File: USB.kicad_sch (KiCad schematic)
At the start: 0 parts

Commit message: [#82055] Add USB recovery port
[#81970] add discharge circuit

[#81970] Annotation

[#81782] Annotation and clean up
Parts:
- added C147: C_1u_25V_0402, antmicro-footprints:C_0402_1005Metric, symbol antmicroCapacitors0402:C_1u_25V_0402
- added C84, C88, C93: C_100n_0402, antmicro-footprints:C_0402_1005Metric, symbol antmicroCapacitors0402:C_100n_0402
- added C91: C_4u7_25V_0402, antmicro-footprints:C_0402_1005Metric, symbol antmicroCapacitors0402:C_4u7_25V_0402
- added C92: C_10u_0402, antmicro-footprints:C_0402_1005Metric, symbol antmicroCapacitors0402:C_10u_0402
- added D19: DF2S30FS_SOD, antmicro-footprints:SOD-923, symbol antmicroTVSDiodes:DF2S30FS_SOD
- added D20: LED_G_0603_LTST-C190GKT, antmicro-footprints:LED_0603_1608Metric_G, symbol antmicroLEDIndicationDiscrete:LED_G_0603_LTST-C190GKT
- added J2: USB-C_GCT_USB4105-GF-A, antmicro-footprints:USB-C_Receptacle_GCT_USB4105-GF-A, symbol antmicroUSBConnectors:USB-C_GCT_USB4105-GF-A
- added Q1: PJE138K, antmicro-footprints:SOT-523, symbol antmicroTransistorsFETsMOSFETsSingle:PJE138K
- added R1: R_4k7_0402, antmicro-footprints:R_0402_1005Metric, symbol antmicroResistors0402:R_4k7_0402
- added R2, R5, R88, R95: R_10k_0402, antmicro-footprints:R_0402_1005Metric, symbol antmicroResistors0402:R_10k_0402
- added R91, R93: R_0R_0402, antmicro-footprints:R_0402_1005Metric, symbol antmicroResistors0402:R_0R_0402
- added R97: R_2k2_0402, antmicro-footprints:R_0402_1005Metric, symbol antmicroResistors0402:R_2k2_0402
- added U1: TPD4E05U06QDQARQ1, antmicro-footprints:USON-10_2.5x1mm_P0.5mm, symbol antmicroTVSDiodes:TPD4E05U06QDQARQ1
- added U16: AP22615A_TSOT26, antmicro-footprints:TSOT23-6, symbol antmicroPMICPowerDistributionSwitchesLoadDrivers:AP22615A_TSOT26
- added U2: TPS65988DHRSHR, antmicro-footprints:IC_TPS65987DDHRSHR, symbol antmicroInterfaceControllers:TPS65988DHRSHR
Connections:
- new net: R93.2, R95.2, U16.4 (EN)
- new net: C147.1, C93.1, D19.1 (C), J2.A4 (VBUS), J2.A9 (VBUS), J2.B4 (VBUS), J2.B9 (VBUS), R1.1, U16.1 (OUT), U2.3 (VBUS2)
- new net: D20.2 (A), R1.2
- new net: J2.A5 (CC_{1}), U1.1, U1.10, U2.45 (C2_CC1)
- new net: J2.B5 (CC_{2}), U1.2, U1.9, U2.47 (C2_CC2)
- new net: U2.52 (DRAIN2), U2.56 (DRAIN2), U2.57 (DRAIN2), U2.7 (DRAIN2)
- new net: R97.2, U16.5 (ISET)
- new net +3V3: R2.2, R88.2
- new net +5V: C88.1, C92.1, R91.2, U16.6 (IN), U2.46 (PP2_CABLE)
- new net FORCE_RECOVERY_N: Q1.3 (D), R2.1
- new net GND: C147.2, C84.2, C88.2, C91.2, C92.2, C93.2, D19.2 (A), D20.1 (C), J2.A1 (GND), J2.A12 (GND), J2.B1 (GND), J2.B12 (GND), J2.SH, Q1.2 (S), R5.1, R95.1, R97.1, U1.3, U1.8, U16.2 (GND)
- new net GPIO21: Q1.1 (G), R5.2, U2.55 (C2_USB_N/GPIO21)
- new net USB0_D+: J2.A6 (D_{A}+), J2.B6 (D_{B}+), U1.4, U1.7
- new net USB0_D-: J2.A7 (D_{A}-), J2.B7 (D_{B}-), U1.5, U1.6
- new net USBC1_5V_PEN: R91.1, R93.1
- new net USBC2_FLG: R88.1, U16.3 (FLG)
- new net USBPD0_HV: C84.1, C91.1, U2.1 (PP_HV2)
- no-connect marks 0 -> 4
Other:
- note added: "USB Port 0 Recovery"

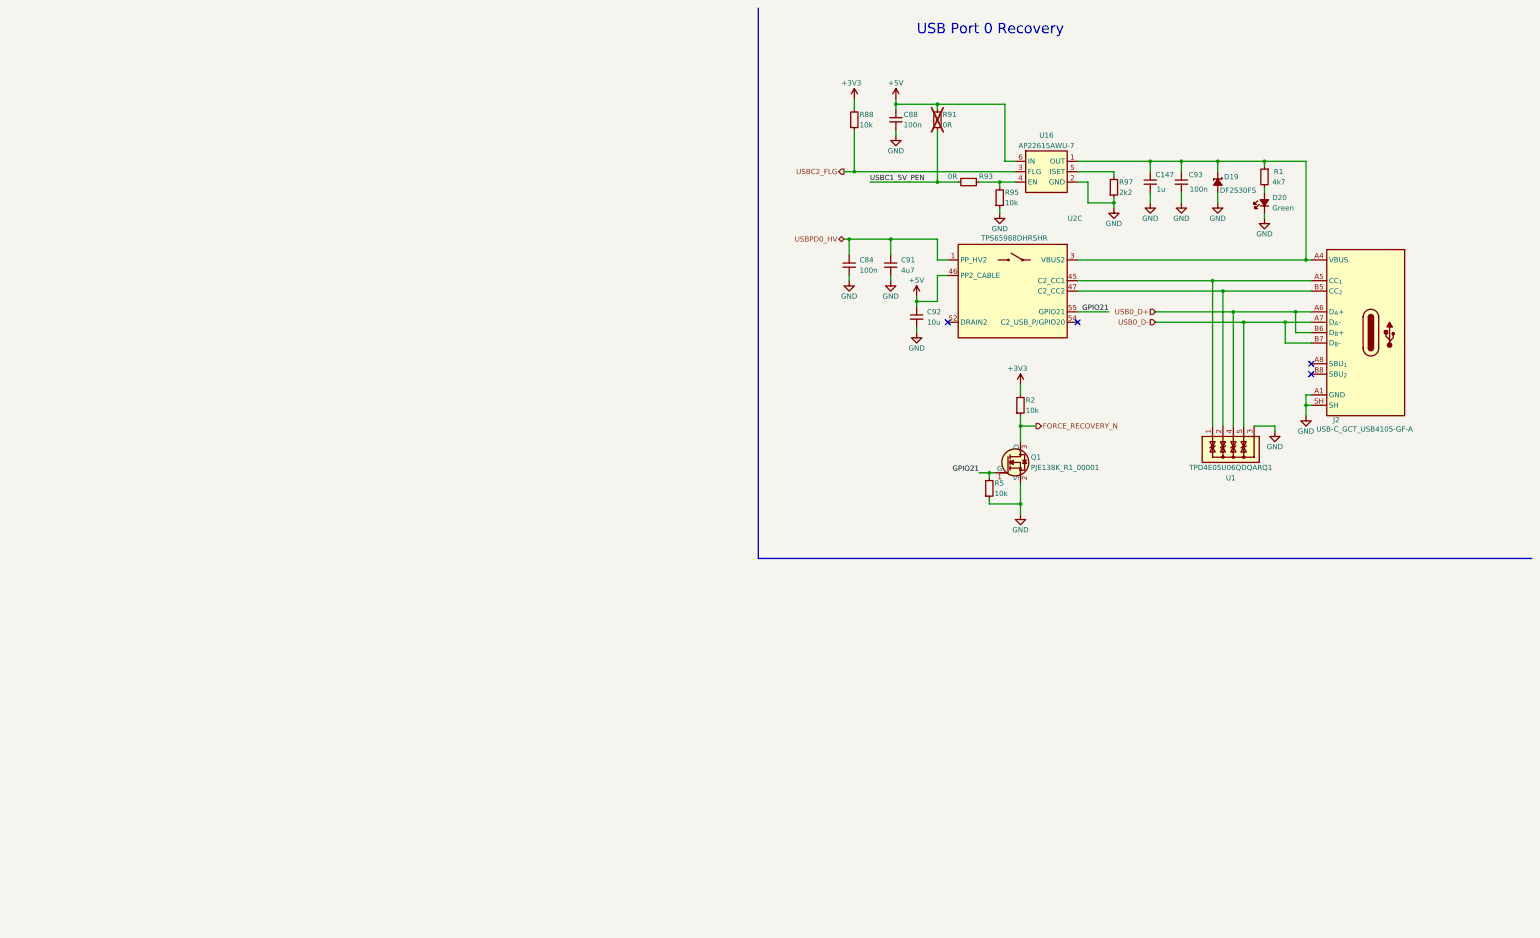
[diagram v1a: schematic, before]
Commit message: [#81970] Finalize connecting SFP+ to SOM
[#82054] Update SoM pins definitions

[#82054] Continue work on I2C

[#82330] Clean up

[#81970] Add SFP sheet and power section

[#82330] Annotation and clean up
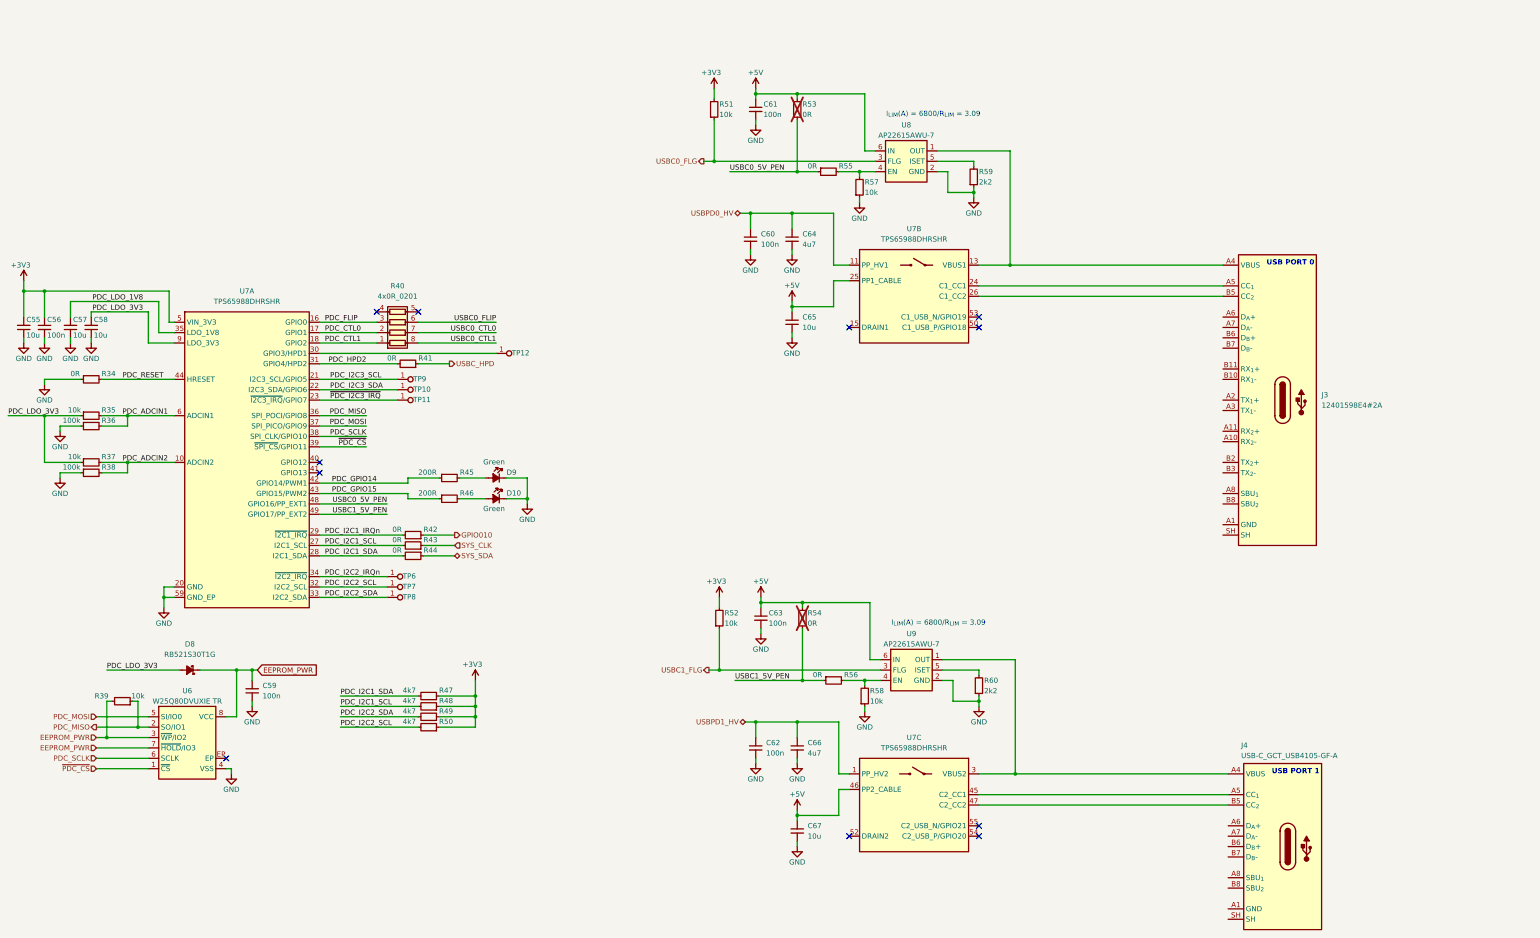
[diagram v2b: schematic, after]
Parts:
- removed C147: C_1u_25V_0402, antmicro-footprints:C_0402_1005Metric, symbol antmicroCapacitors0402:C_1u_25V_0402
- removed C93: C_100n_0402, antmicro-footprints:C_0402_1005Metric, symbol antmicroCapacitors0402:C_100n_0402
- removed D19: DF2S30FS_SOD, antmicro-footprints:SOD-923, symbol antmicroTVSDiodes:DF2S30FS_SOD
- removed D20: LED_G_0603_LTST-C190GKT, antmicro-footprints:LED_0603_1608Metric_G, symbol antmicroLEDIndicationDiscrete:LED_G_0603_LTST-C190GKT
- removed J2: USB-C_GCT_USB4105-GF-A, antmicro-footprints:USB-C_Receptacle_GCT_USB4105-GF-A, symbol antmicroUSBConnectors:USB-C_GCT_USB4105-GF-A
- removed Q1: PJE138K, antmicro-footprints:SOT-523, symbol antmicroTransistorsFETsMOSFETsSingle:PJE138K
- removed R1: R_4k7_0402, antmicro-footprints:R_0402_1005Metric, symbol antmicroResistors0402:R_4k7_0402
- removed R2, R5: R_10k_0402, antmicro-footprints:R_0402_1005Metric, symbol antmicroResistors0402:R_10k_0402
- removed R97: R_2k2_0402, antmicro-footprints:R_0402_1005Metric, symbol antmicroResistors0402:R_2k2_0402
- removed U1: TPD4E05U06QDQARQ1, antmicro-footprints:USON-10_2.5x1mm_P0.5mm, symbol antmicroTVSDiodes:TPD4E05U06QDQARQ1
- removed U2: TPS65988DHRSHR, antmicro-footprints:IC_TPS65987DDHRSHR, symbol antmicroInterfaceControllers:TPS65988DHRSHR
- added C55, C57, C58, C65: C_10u_0402, antmicro-footprints:C_0402_1005Metric, symbol antmicroCapacitors0402:C_10u_0402
- added C56, C59, C60, C61: C_100n_0402, antmicro-footprints:C_0402_1005Metric, symbol antmicroCapacitors0402:C_100n_0402
- added C64: C_4u7_25V_0402, antmicro-footprints:C_0402_1005Metric, symbol antmicroCapacitors0402:C_4u7_25V_0402
- added D10, D9: LED_G_0603_LTST-C190GKT, antmicro-footprints:LED_0603_1608Metric_G, symbol antmicroLEDIndicationDiscrete:LED_G_0603_LTST-C190GKT
- added D8: RB521S30T1G, antmicro-footprints:SOD-523, symbol antmicroDiodesRectifiersSingle:RB521S30T1G
- added J3: USB-C_Amphenol_12401598E4, antmicro-footprints:USB-C_Receptacle_Amphenol_12401598E4, symbol antmicroUSBConnectors:USB-C_Amphenol_12401598E4
- added J4: USB-C_GCT_USB4105-GF-A, antmicro-footprints:USB-C_Receptacle_GCT_USB4105-GF-A, symbol antmicroUSBConnectors:USB-C_GCT_USB4105-GF-A
- added R34, R41, R42, R43, R44, R53, R55: R_0R_0402, antmicro-footprints:R_0402_1005Metric, symbol antmicroResistors0402:R_0R_0402
- added R35, R37, R39, R51, R57: R_10k_0402, antmicro-footprints:R_0402_1005Metric, symbol antmicroResistors0402:R_10k_0402
- added R36, R38: R_100k_0402, antmicro-footprints:R_0402_1005Metric, symbol antmicroResistors0402:R_100k_0402
- added R40: R_4x0R_0201_array, antmicro-footprints:R_Array_4x0201_Panasonic_EXB18V, symbol antmicroResistorNetworksArrays:R_4x0R_0201_array
- added R45, R46: R_200R_0402, antmicro-footprints:R_0402_1005Metric, symbol antmicroResistors0402:R_200R_0402
- added R47, R48, R49, R50: R_4k7_0402, antmicro-footprints:R_0402_1005Metric, symbol antmicroResistors0402:R_4k7_0402
- added R59, R60: R_2k2_0402, antmicro-footprints:R_0402_1005Metric, symbol antmicroResistors0402:R_2k2_0402
- added TP10, TP11, TP12, TP6, TP7, TP8, TP9: TP_0.75mm_SMD, antmicro-footprints:TP_SMD_0.75mm, symbol antmicroTestPoints:TP_0.75mm_SMD
- added U6: W25Q80DV_USON, antmicro-footprints:USON-8_2x3mm_P0.5mm, symbol antmicroMemory:W25Q80DV_USON
- added U7: TPS65988DHRSHR, antmicro-footprints:IC_TPS65987DDHRSHR, symbol antmicroInterfaceControllers:TPS65988DHRSHR
- added U8: AP22615A_TSOT26, antmicro-footprints:TSOT23-6, symbol antmicroPMICPowerDistributionSwitchesLoadDrivers:AP22615A_TSOT26
- renumbered C84 to C62, C88 to C63, C91 to C66, C92 to C67, R88 to R52, R91 to R54, R93 to R56, R95 to R58, U16 to U9
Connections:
- net +3V3: now also C55.2, C56.1, R47.1, R48.1, R49.1, R50.1, R51.2, U7.5 (VIN_3V3)
- net +5V: now also C61.1, C65.1, R53.2, U7.25 (PP1_CABLE), U7.46 (PP2_CABLE), U8.6 (IN)
- net GND: now also C55.1, C56.2, C57.1, C58.1, C59.1, C60.2, C61.2, C64.2, C65.2, D10.1 (C), D9.1 (C), R34.1, R36.1, R38.1, R57.1, R59.1, R60.1, U6.4 (VSS), U7.20 (GND), U7.51 (GND), U7.59 (GND_EP), U8.2 (GND)
- net USBC1_5V_PEN: now also U7.49 (GPIO17/PP_EXT2)
- net USBPD0_HV: now also C60.1, C64.1, U7.11 (PP_HV1); no longer C62.1, C66.1
- net at U9.1 (OUT): now also J4.A4 (VBUS), J4.A9 (VBUS), J4.B4 (VBUS), J4.B9 (VBUS), U7.3 (VBUS2)
- net at U9.5 (ISET): now also R60.2
- net USBC2_FLG renamed USBC1_FLG
- new net: R59.2, U8.5 (ISET)
- new net: D9.2 (A), R45.2
- new net: J3.A4 (VBUS), J3.A9 (VBUS), J3.B4 (VBUS), J3.B9 (VBUS), U7.13 (VBUS1), U8.1 (OUT)
- new net: R55.2, R57.2, U8.4 (EN)
- new net: TP12.1, U7.30 (GPIO3/HPD1)
- new net: U7.15 (DRAIN1), U7.19 (DRAIN1), U7.58 (DRAIN1), U7.8 (DRAIN1)
- new net: J3.A5 (CC_{1}), U7.24 (C1_CC1)
- new net: J3.B5 (CC_{2}), U7.26 (C1_CC2)
- new net: J3.A1 (GND), J3.A12 (GND), J3.B1 (GND), J3.B12 (GND)
- new net: D10.2 (A), R46.2
- new net: J4.A1 (GND), J4.A12 (GND), J4.B1 (GND), J4.B12 (GND)
- new net: J4.A5 (CC_{1}), U7.45 (C2_CC1)
- new net: J4.B5 (CC_{2}), U7.47 (C2_CC2)
- new net: U7.52 (DRAIN2), U7.56 (DRAIN2), U7.57 (DRAIN2), U7.7 (DRAIN2)
- new net EEPROM_PWR: C59.2, D8.1 (C), R39.2, U6.3 (~{WP}/IO2), U6.7 (~{HOLD}/IO3), U6.8 (VCC)
- new net GPIO010: R42.1
- new net PDC_ADCIN1: R35.2, R36.2, U7.6 (ADCIN1)
- new net PDC_ADCIN2: R37.2, R38.2, U7.10 (ADCIN2)
- new net PDC_CTL0: R40.2 (R2.1), U7.17 (GPIO1)
- new net PDC_CTL1: R40.1 (R1.1), U7.18 (GPIO2)
- new net PDC_FLIP: R40.3 (R3.1), U7.16 (GPIO0)
- new net PDC_GPIO14: R45.1, U7.42 (GPIO14/PWM1)
- new net PDC_GPIO15: R46.1, U7.43 (GPIO15/PWM2)
- new net PDC_HPD2: R41.2, U7.31 (GPIO4/HPD2)
- new net PDC_I2C1_IRQn: R42.2, U7.29 (~{I2C1_IRQ})
- new net PDC_I2C1_SCL: R43.2, R48.2, U7.27 (I2C1_SCL)
- new net PDC_I2C1_SDA: R44.2, R47.2, U7.28 (I2C1_SDA)
- new net PDC_I2C2_IRQn: TP6.1, U7.34 (~{I2C2_IRQ})
- new net PDC_I2C2_SCL: R50.2, TP7.1, U7.32 (I2C2_SCL)
- new net PDC_I2C2_SDA: R49.2, TP8.1, U7.33 (I2C2_SDA)
- new net PDC_I2C3_SCL: TP9.1, U7.21 (I2C3_SCL/GPIO5)
- new net PDC_I2C3_SDA: TP10.1, U7.22 (I2C3_SDA/GPIO6)
- new net PDC_LDO_1V8: C57.2, U7.35 (LDO_1V8)
- new net PDC_LDO_3V3: C58.2, D8.2 (A), R35.1, R37.1, U7.9 (LDO_3V3)
- new net PDC_MISO: R39.1, U6.2 (SO/IO1), U7.36 (SPI_POCI/GPIO8)
- new net PDC_MOSI: U6.5 (SI/IO0), U7.37 (SPI_PICO/GPIO9)
- new net PDC_RESET: R34.2, U7.44 (HRESET)
- new net PDC_SCLK: U6.6 (SCLK), U7.38 (SPI_CLK/GPIO10)
- new net SYS_CLK: R43.1
- new net SYS_SDA: R44.1
- new net USBC0_5V_PEN: R53.1, R55.1, U7.48 (GPIO16/PP_EXT1)
- new net USBC0_CTL0: R40.7 (R2.2)
- new net USBC0_CTL1: R40.8 (R1.2)
- new net USBC0_FLG: R51.1, U8.3 (FLG)
- new net USBC0_FLIP: R40.6 (R3.2)
- new net USBC_HPD: R41.1
- new net USBPD1_HV: C62.1, C66.1, U7.1 (PP_HV2)
- new net ~{PDC_CS}: U6.1 (~{CS}), U7.39 (~{SPI_CS}/GPIO11)
- new net ~{PDC_I2C3_IRQ}: TP11.1, U7.23 (~{I2C3_IRQ}/GPIO7)
- no-connect marks 4 -> 11
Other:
- note added: "I_{LIM}(A) = 6800/R_{LIM} = 3.09"
- note added: "USB PORT 0"
- note added: "USB PORT 1"
- note removed: "USB Port 0 Recovery"
- moved on the sheet: C62, C63, C66, C67, R52, R54, R56, R58, U9

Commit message: [#82055] Revert back to USB-PD on DP and Debug ports
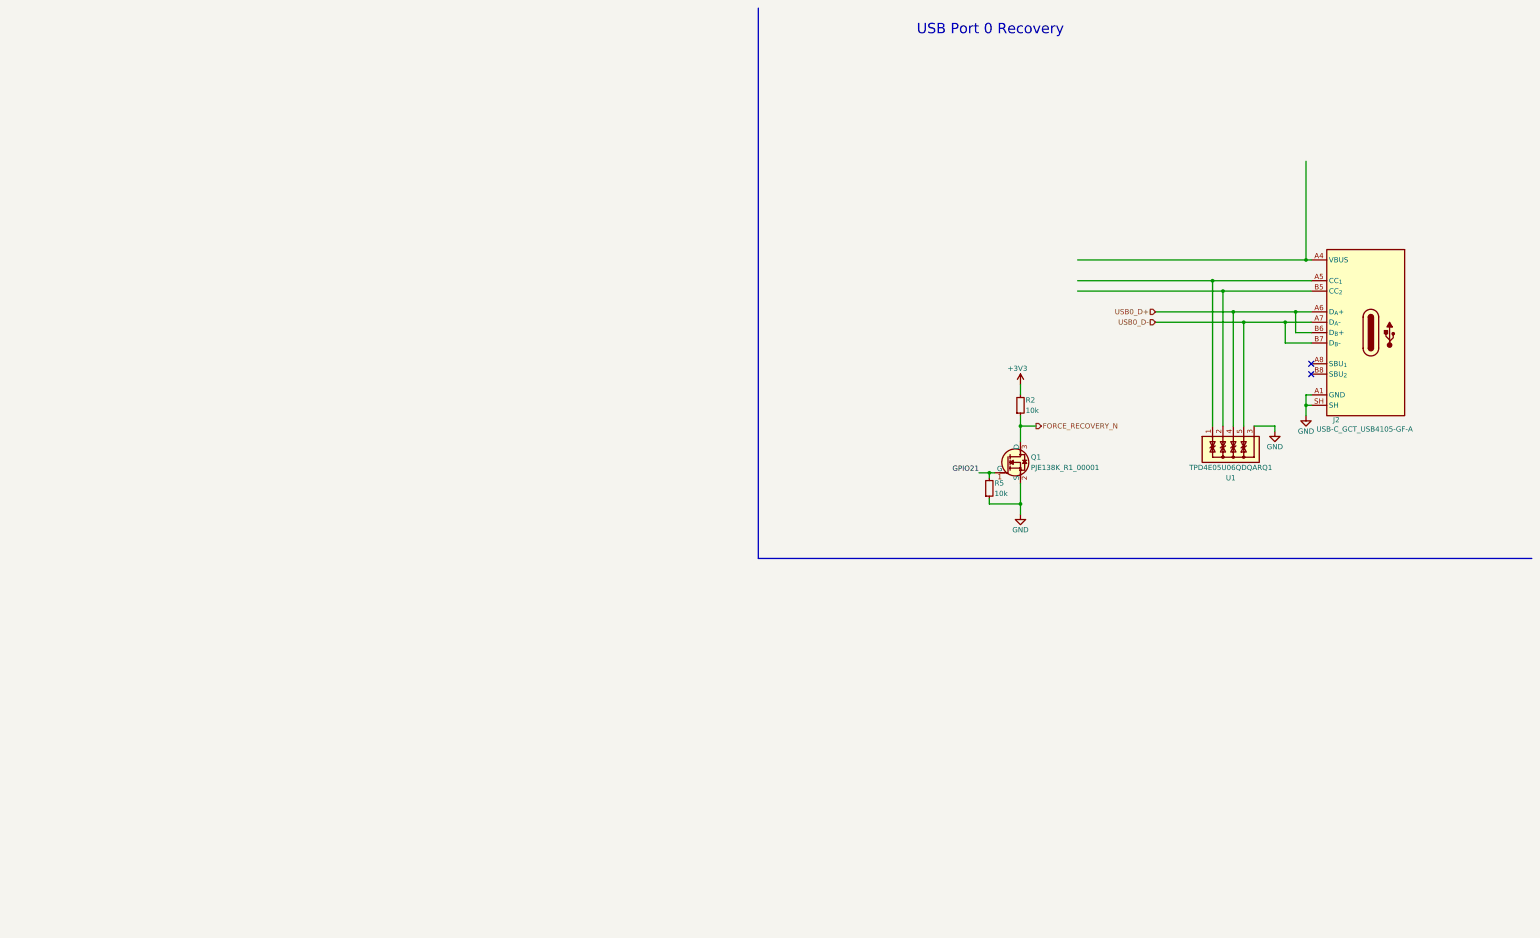
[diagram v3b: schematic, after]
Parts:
- removed C55, C57, C58, C65, C67: C_10u_0402, antmicro-footprints:C_0402_1005Metric, symbol antmicroCapacitors0402:C_10u_0402
- removed C56, C59, C60, C61, C62, C63: C_100n_0402, antmicro-footprints:C_0402_1005Metric, symbol antmicroCapacitors0402:C_100n_0402
- removed C64, C66: C_4u7_25V_0402, antmicro-footprints:C_0402_1005Metric, symbol antmicroCapacitors0402:C_4u7_25V_0402
- removed D10, D9: LED_G_0603_LTST-C190GKT, antmicro-footprints:LED_0603_1608Metric_G, symbol antmicroLEDIndicationDiscrete:LED_G_0603_LTST-C190GKT
- removed D8: RB521S30T1G, antmicro-footprints:SOD-523, symbol antmicroDiodesRectifiersSingle:RB521S30T1G
- removed J3: USB-C_Amphenol_12401598E4, antmicro-footprints:USB-C_Receptacle_Amphenol_12401598E4, symbol antmicroUSBConnectors:USB-C_Amphenol_12401598E4
- removed J4: USB-C_GCT_USB4105-GF-A, antmicro-footprints:USB-C_Receptacle_GCT_USB4105-GF-A, symbol antmicroUSBConnectors:USB-C_GCT_USB4105-GF-A
- removed R34, R41, R42, R43, R44, R53, R54, R55, R56: R_0R_0402, antmicro-footprints:R_0402_1005Metric, symbol antmicroResistors0402:R_0R_0402
- removed R35, R37, R39, R51, R52, R57, R58: R_10k_0402, antmicro-footprints:R_0402_1005Metric, symbol antmicroResistors0402:R_10k_0402
- removed R36, R38: R_100k_0402, antmicro-footprints:R_0402_1005Metric, symbol antmicroResistors0402:R_100k_0402
- removed R40: R_4x0R_0201_array, antmicro-footprints:R_Array_4x0201_Panasonic_EXB18V, symbol antmicroResistorNetworksArrays:R_4x0R_0201_array
- removed R45, R46: R_200R_0402, antmicro-footprints:R_0402_1005Metric, symbol antmicroResistors0402:R_200R_0402
- removed R47, R48, R49, R50: R_4k7_0402, antmicro-footprints:R_0402_1005Metric, symbol antmicroResistors0402:R_4k7_0402
- removed R59, R60: R_2k2_0402, antmicro-footprints:R_0402_1005Metric, symbol antmicroResistors0402:R_2k2_0402
- removed TP10, TP11, TP12, TP6, TP7, TP8, TP9: TP_0.75mm_SMD, antmicro-footprints:TP_SMD_0.75mm, symbol antmicroTestPoints:TP_0.75mm_SMD
- removed U6: W25Q80DV_USON, antmicro-footprints:USON-8_2x3mm_P0.5mm, symbol antmicroMemory:W25Q80DV_USON
- removed U7: TPS65988DHRSHR, antmicro-footprints:IC_TPS65987DDHRSHR, symbol antmicroInterfaceControllers:TPS65988DHRSHR
- removed U8, U9: AP22615A_TSOT26, antmicro-footprints:TSOT23-6, symbol antmicroPMICPowerDistributionSwitchesLoadDrivers:AP22615A_TSOT26
- added J2: USB-C_GCT_USB4105-GF-A, antmicro-footprints:USB-C_Receptacle_GCT_USB4105-GF-A, symbol antmicroUSBConnectors:USB-C_GCT_USB4105-GF-A
- added Q1: PJE138K, antmicro-footprints:SOT-523, symbol antmicroTransistorsFETsMOSFETsSingle:PJE138K
- added R2, R5: R_10k_0402, antmicro-footprints:R_0402_1005Metric, symbol antmicroResistors0402:R_10k_0402
- added U1: TPD4E05U06QDQARQ1, antmicro-footprints:USON-10_2.5x1mm_P0.5mm, symbol antmicroTVSDiodes:TPD4E05U06QDQARQ1
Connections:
- net +3V3: now also R2.2
- net GND: now also J2.A1 (GND), J2.A12 (GND), J2.B1 (GND), J2.B12 (GND), J2.SH, Q1.2 (S), R5.1, U1.3, U1.8
- new net: J2.A4 (VBUS), J2.A9 (VBUS), J2.B4 (VBUS), J2.B9 (VBUS)
- new net: J2.A5 (CC_{1}), U1.1, U1.10
- new net: J2.B5 (CC_{2}), U1.2, U1.9
- new net FORCE_RECOVERY_N: Q1.3 (D), R2.1
- new net GPIO21: Q1.1 (G), R5.2
- new net USB0_D+: J2.A6 (D_{A}+), J2.B6 (D_{B}+), U1.4, U1.7
- new net USB0_D-: J2.A7 (D_{A}-), J2.B7 (D_{B}-), U1.5, U1.6
- no-connect marks 11 -> 2
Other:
- note added: "USB Port 0 Recovery"
- note removed: "I_{LIM}(A) = 6800/R_{LIM} = 3.09"
- note removed: "USB PORT 0"
- note removed: "USB PORT 1"
